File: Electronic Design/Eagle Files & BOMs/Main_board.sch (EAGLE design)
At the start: 36 parts, among them IC1 ACS712ELC-5A, IC2 ATMEGA328-PU, Q1 IRF9540, Q2 IRF9540, X1 16MHz

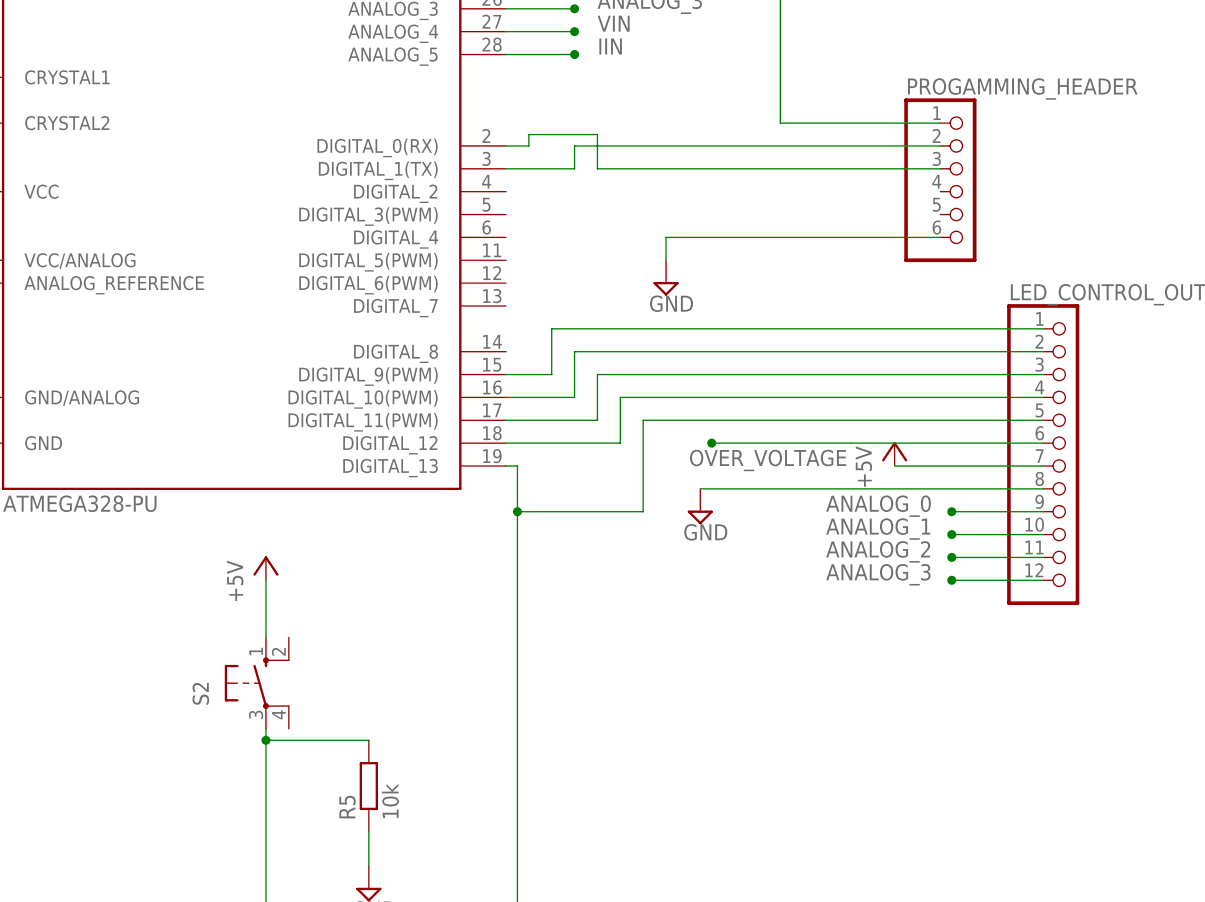
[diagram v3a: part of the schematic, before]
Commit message: adding header for additional DIO pins
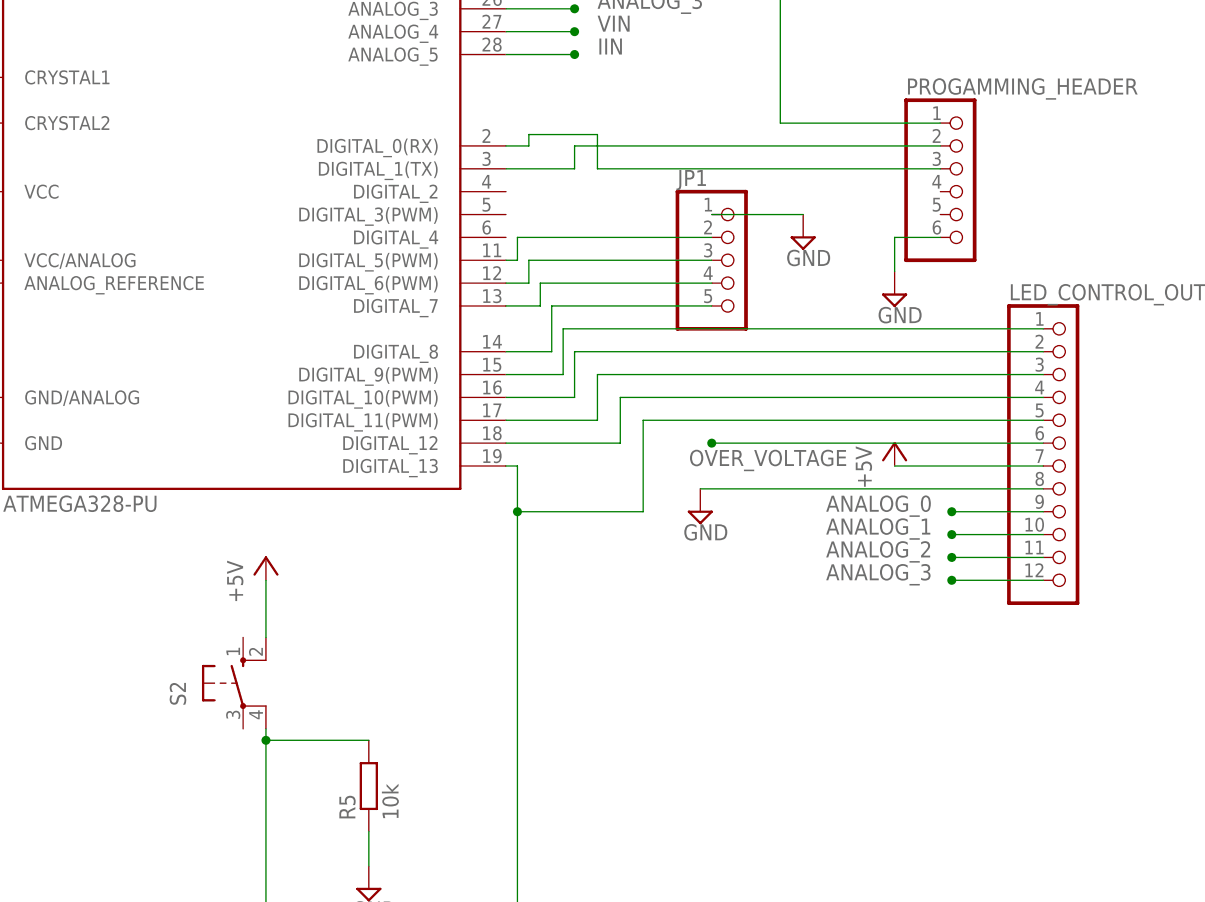
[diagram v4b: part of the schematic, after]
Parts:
- added JP1: (no value), pinhead:PINHD-1X5
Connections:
- new net N$20: IC2.DIGITAL_8, JP1.5
- new net N$21: IC2.DIGITAL_7, JP1.4
- new net N$22: IC2.DIGITAL_6(PWM), JP1.3
- new net N$25: IC2.DIGITAL_5(PWM), JP1.2
- net +5V: now also S2.S1; no longer S2.S
- net GND: now also JP1.1
- net N$8: now also S2.P1; no longer S2.P
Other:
- moved on the sheet: S2
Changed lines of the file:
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@@
 <part name="SUPPLY4" library="supply2" deviceset="GND" device=""/>
 <part name="R6" library="varistor" deviceset="S14K17" device="" value="S14K75"/>
+<part name="JP1" library="pinhead" deviceset="PINHD-1X5" device=""/>
+<part name="SUPPLY5" library="supply2" deviceset="GND" device=""/>
 </parts>
 <sheets>
@@
 <instance part="+3V3" gate="1" x="31.75" y="113.03"/>
 <instance part="PROGAMMING_HEADER" gate="A" x="38.1" y="22.86"/>
-<instance part="SUPPLY6" gate="GND" x="5.08" y="12.7"/>
+<instance part="SUPPLY6" gate="GND" x="30.48" y="11.43"/>
 <instance part="C6" gate="G$1" x="74.93" y="50.8"/>
 <instance part="VIN_BUCK/BOOST" gate="A" x="115.57" y="93.98"/>
@@
 <instance part="R3" gate="G$1" x="77.47" y="99.06"/>
 <instance part="USB_OUT" gate="A" x="93.98" y="87.63"/>
-<instance part="S2" gate="1" x="-39.37" y="-31.75"/>
+<instance part="S2" gate="1" x="-41.91" y="-31.75"/>
 <instance part="+5V2" gate="1" x="-39.37" y="-17.78"/>
 <instance part="R5" gate="G$1" x="-27.94" y="-43.18" rot="R90"/>
@@
 <instance part="SUPPLY4" gate="GND" x="104.14" y="69.85"/>
 <instance part="R6" gate="G$1" x="-97.79" y="88.9" rot="R270"/>
+<instance part="JP1" gate="A" x="12.7" y="15.24"/>
+<instance part="SUPPLY5" gate="GND" x="20.32" y="17.78"/>
 </instances>
 <busses>
@@
 <segment>
 <pinref part="PROGAMMING_HEADER" gate="A" pin="6"/>
-<wire x1="35.56" y1="17.78" x2="5.08" y2="17.78" width="0.1524" layer="91"/>
-<wire x1="5.08" y1="17.78" x2="5.08" y2="15.24" width="0.1524" layer="91"/>
+<wire x1="35.56" y1="17.78" x2="30.48" y2="17.78" width="0.1524" layer="91"/>
+<wire x1="30.48" y1="17.78" x2="30.48" y2="13.97" width="0.1524" layer="91"/>
 <pinref part="SUPPLY6" gate="GND" pin="GND"/>
 </segment>
@@
 <pinref part="VIN_BUCK/BOOST" gate="A" pin="3"/>
 <wire x1="113.03" y1="91.44" x2="104.14" y2="91.44" width="0.1524" layer="91"/>
+</segment>
+<segment>
+<pinref part="JP1" gate="A" pin="1"/>
+<pinref part="SUPPLY5" gate="GND" pin="GND"/>
+<wire x1="10.16" y1="20.32" x2="20.32" y2="20.32" width="0.1524" layer="91"/>
 </segment>
 </net>
@@
 </segment>
 <segment>
-<pinref part="S2" gate="1" pin="S"/>
-<pinref part="+5V2" gate="1" pin="+5V"/>
-<wire x1="-39.37" y1="-26.67" x2="-39.37" y2="-20.32" width="0.1524" layer="91"/>
-</segment>
-<segment>
 <pinref part="+5V3" gate="1" pin="+5V"/>
 <pinref part="LED_CONTROL_OUT" gate="G$1" pin="7"/>
@@
 <wire x1="13.97" y1="105.41" x2="31.75" y2="105.41" width="0.1524" layer="91"/>
 <pinref part="+3V3" gate="1" pin="+5V"/>
+</segment>
+<segment>
+<pinref part="+5V2" gate="1" pin="+5V"/>
+<pinref part="S2" gate="1" pin="S1"/>
+<wire x1="-39.37" y1="-20.32" x2="-39.37" y2="-26.67" width="0.1524" layer="91"/>
 </segment>
 </net>
@@
 <wire x1="-12.7" y1="-7.62" x2="-11.43" y2="-7.62" width="0.1524" layer="91"/>
 <wire x1="-11.43" y1="-7.62" x2="-11.43" y2="-12.7" width="0.1524" layer="91"/>
-<pinref part="S2" gate="1" pin="P"/>
 <wire x1="-11.43" y1="-12.7" x2="-11.43" y2="-68.58" width="0.1524" layer="91"/>
 <wire x1="-11.43" y1="-68.58" x2="-39.37" y2="-68.58" width="0.1524" layer="91"/>
 <wire x1="-39.37" y1="-68.58" x2="-39.37" y2="-38.1" width="0.1524" layer="91"/>
 <pinref part="R5" gate="G$1" pin="2"/>
-<wire x1="-39.37" y1="-38.1" x2="-39.37" y2="-36.83" width="0.1524" layer="91"/>
 <wire x1="-27.94" y1="-38.1" x2="-39.37" y2="-38.1" width="0.1524" layer="91"/>
-<junction x="-39.37" y="-38.1"/>
 <wire x1="2.54" y1="-2.54" x2="2.54" y2="-12.7" width="0.1524" layer="91"/>
 <wire x1="2.54" y1="-12.7" x2="-11.43" y2="-12.7" width="0.1524" layer="91"/>
@@
 <pinref part="LED_CONTROL_OUT" gate="G$1" pin="5"/>
 <wire x1="46.99" y1="-2.54" x2="2.54" y2="-2.54" width="0.1524" layer="91"/>
+<pinref part="S2" gate="1" pin="P1"/>
+<wire x1="-39.37" y1="-36.83" x2="-39.37" y2="-38.1" width="0.1524" layer="91"/>
+<junction x="-39.37" y="-38.1"/>
 </segment>
 </net>
@@
 <segment>
 <pinref part="IC2" gate="1" pin="DIGITAL_9(PWM)"/>
-<wire x1="-12.7" y1="2.54" x2="-7.62" y2="2.54" width="0.1524" layer="91"/>
-<wire x1="-7.62" y1="2.54" x2="-7.62" y2="7.62" width="0.1524" layer="91"/>
+<wire x1="-12.7" y1="2.54" x2="-6.35" y2="2.54" width="0.1524" layer="91"/>
+<wire x1="-6.35" y1="2.54" x2="-6.35" y2="7.62" width="0.1524" layer="91"/>
 <pinref part="LED_CONTROL_OUT" gate="G$1" pin="1"/>
-<wire x1="-7.62" y1="7.62" x2="46.99" y2="7.62" width="0.1524" layer="91"/>
+<wire x1="-6.35" y1="7.62" x2="46.99" y2="7.62" width="0.1524" layer="91"/>
 </segment>
 </net>
@@
 </segment>
 </net>
+<net name="N$20" class="0">
+<segment>
+<pinref part="IC2" gate="1" pin="DIGITAL_8"/>
+<wire x1="-7.62" y1="5.08" x2="-12.7" y2="5.08" width="0.1524" layer="91"/>
+<pinref part="JP1" gate="A" pin="5"/>
+<wire x1="10.16" y1="10.16" x2="-7.62" y2="10.16" width="0.1524" layer="91"/>
+<wire x1="-7.62" y1="10.16" x2="-7.62" y2="5.08" width="0.1524" layer="91"/>
+</segment>
+</net>
+<net name="N$21" class="0">
+<segment>
+<pinref part="IC2" gate="1" pin="DIGITAL_7"/>
+<wire x1="-8.89" y1="10.16" x2="-12.7" y2="10.16" width="0.1524" layer="91"/>
+<wire x1="-8.89" y1="10.16" x2="-8.89" y2="12.7" width="0.1524" layer="91"/>
+<pinref part="JP1" gate="A" pin="4"/>
+<wire x1="-8.89" y1="12.7" x2="10.16" y2="12.7" width="0.1524" layer="91"/>
+</segment>
+</net>
+<net name="N$22" class="0">
+<segment>
+<pinref part="IC2" gate="1" pin="DIGITAL_6(PWM)"/>
+<wire x1="-12.7" y1="12.7" x2="-10.16" y2="12.7" width="0.1524" layer="91"/>
+<wire x1="-10.16" y1="12.7" x2="-10.16" y2="15.24" width="0.1524" layer="91"/>
+<pinref part="JP1" gate="A" pin="3"/>
+<wire x1="-10.16" y1="15.24" x2="10.16" y2="15.24" width="0.1524" layer="91"/>
+</segment>
+</net>
+<net name="N$25" class="0">
+<segment>
+<pinref part="IC2" gate="1" pin="DIGITAL_5(PWM)"/>
+<wire x1="-12.7" y1="15.24" x2="-11.43" y2="15.24" width="0.1524" layer="91"/>
+<wire x1="-11.43" y1="15.24" x2="-11.43" y2="17.78" width="0.1524" layer="91"/>
+<pinref part="JP1" gate="A" pin="2"/>
+<wire x1="-11.43" y1="17.78" x2="10.16" y2="17.78" width="0.1524" layer="91"/>
+</segment>
+</net>

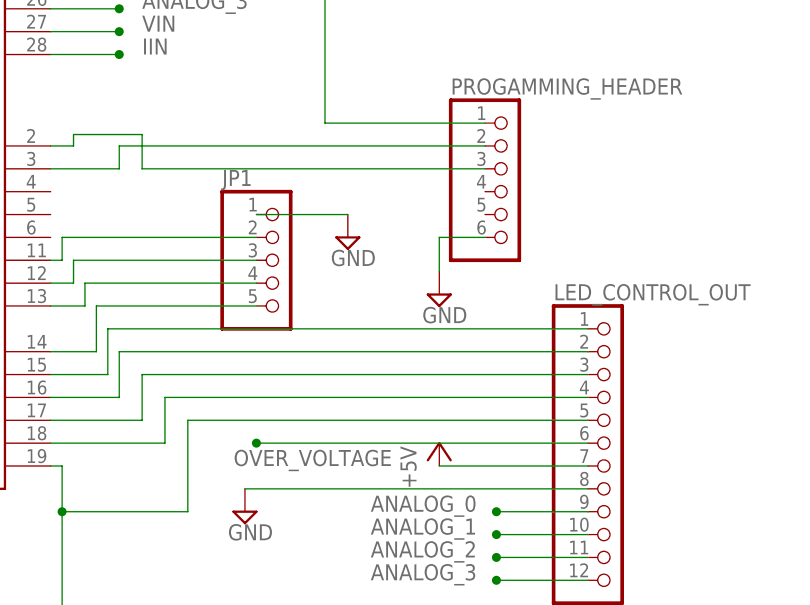
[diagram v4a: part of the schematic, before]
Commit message: fixing minor drc errors and repostionings monting holes
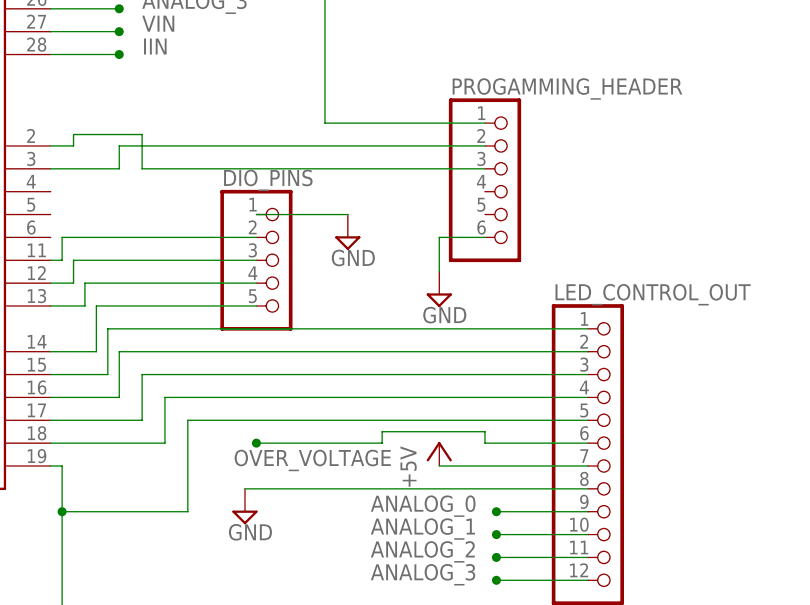
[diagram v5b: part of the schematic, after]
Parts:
- renumbered JP1 to DIO_PINS
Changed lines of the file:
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@@
 <part name="SUPPLY4" library="supply2" deviceset="GND" device=""/>
 <part name="R6" library="varistor" deviceset="S14K17" device="" value="S14K75"/>
-<part name="JP1" library="pinhead" deviceset="PINHD-1X5" device=""/>
+<part name="DIO_PINS" library="pinhead" deviceset="PINHD-1X5" device=""/>
 <part name="SUPPLY5" library="supply2" deviceset="GND" device=""/>
 </parts>
@@
 <instance part="SUPPLY4" gate="GND" x="104.14" y="69.85"/>
 <instance part="R6" gate="G$1" x="-97.79" y="88.9" rot="R270"/>
-<instance part="JP1" gate="A" x="12.7" y="15.24"/>
+<instance part="DIO_PINS" gate="A" x="12.7" y="15.24"/>
 <instance part="SUPPLY5" gate="GND" x="20.32" y="17.78"/>
 </instances>
@@
 </segment>
 <segment>
-<pinref part="JP1" gate="A" pin="1"/>
+<pinref part="DIO_PINS" gate="A" pin="1"/>
 <pinref part="SUPPLY5" gate="GND" pin="GND"/>
 <wire x1="10.16" y1="20.32" x2="20.32" y2="20.32" width="0.1524" layer="91"/>
@@
 <segment>
 <pinref part="LED_CONTROL_OUT" gate="G$1" pin="6"/>
-<wire x1="46.99" y1="-5.08" x2="10.16" y2="-5.08" width="0.1524" layer="91"/>
+<wire x1="46.99" y1="-5.08" x2="35.56" y2="-5.08" width="0.1524" layer="91"/>
 <junction x="10.16" y="-5.08"/>
 <label x="7.62" y="-7.62" size="1.778" layer="95"/>
+<wire x1="24.13" y1="-5.08" x2="10.16" y2="-5.08" width="0.1524" layer="91"/>
+<wire x1="35.56" y1="-5.08" x2="35.56" y2="-3.81" width="0.1524" layer="91"/>
+<wire x1="35.56" y1="-3.81" x2="24.13" y2="-3.81" width="0.1524" layer="91"/>
+<wire x1="24.13" y1="-3.81" x2="24.13" y2="-5.08" width="0.1524" layer="91"/>
 </segment>
 <segment>
@@
 <pinref part="IC2" gate="1" pin="DIGITAL_8"/>
 <wire x1="-7.62" y1="5.08" x2="-12.7" y2="5.08" width="0.1524" layer="91"/>
-<pinref part="JP1" gate="A" pin="5"/>
+<pinref part="DIO_PINS" gate="A" pin="5"/>
 <wire x1="10.16" y1="10.16" x2="-7.62" y2="10.16" width="0.1524" layer="91"/>
 <wire x1="-7.62" y1="10.16" x2="-7.62" y2="5.08" width="0.1524" layer="91"/>
@@
 <wire x1="-8.89" y1="10.16" x2="-12.7" y2="10.16" width="0.1524" layer="91"/>
 <wire x1="-8.89" y1="10.16" x2="-8.89" y2="12.7" width="0.1524" layer="91"/>
-<pinref part="JP1" gate="A" pin="4"/>
+<pinref part="DIO_PINS" gate="A" pin="4"/>
 <wire x1="-8.89" y1="12.7" x2="10.16" y2="12.7" width="0.1524" layer="91"/>
 </segment>
@@
 <wire x1="-12.7" y1="12.7" x2="-10.16" y2="12.7" width="0.1524" layer="91"/>
 <wire x1="-10.16" y1="12.7" x2="-10.16" y2="15.24" width="0.1524" layer="91"/>
-<pinref part="JP1" gate="A" pin="3"/>
+<pinref part="DIO_PINS" gate="A" pin="3"/>
 <wire x1="-10.16" y1="15.24" x2="10.16" y2="15.24" width="0.1524" layer="91"/>
 </segment>
@@
 <wire x1="-12.7" y1="15.24" x2="-11.43" y2="15.24" width="0.1524" layer="91"/>
 <wire x1="-11.43" y1="15.24" x2="-11.43" y2="17.78" width="0.1524" layer="91"/>
-<pinref part="JP1" gate="A" pin="2"/>
+<pinref part="DIO_PINS" gate="A" pin="2"/>
 <wire x1="-11.43" y1="17.78" x2="10.16" y2="17.78" width="0.1524" layer="91"/>
 </segment>

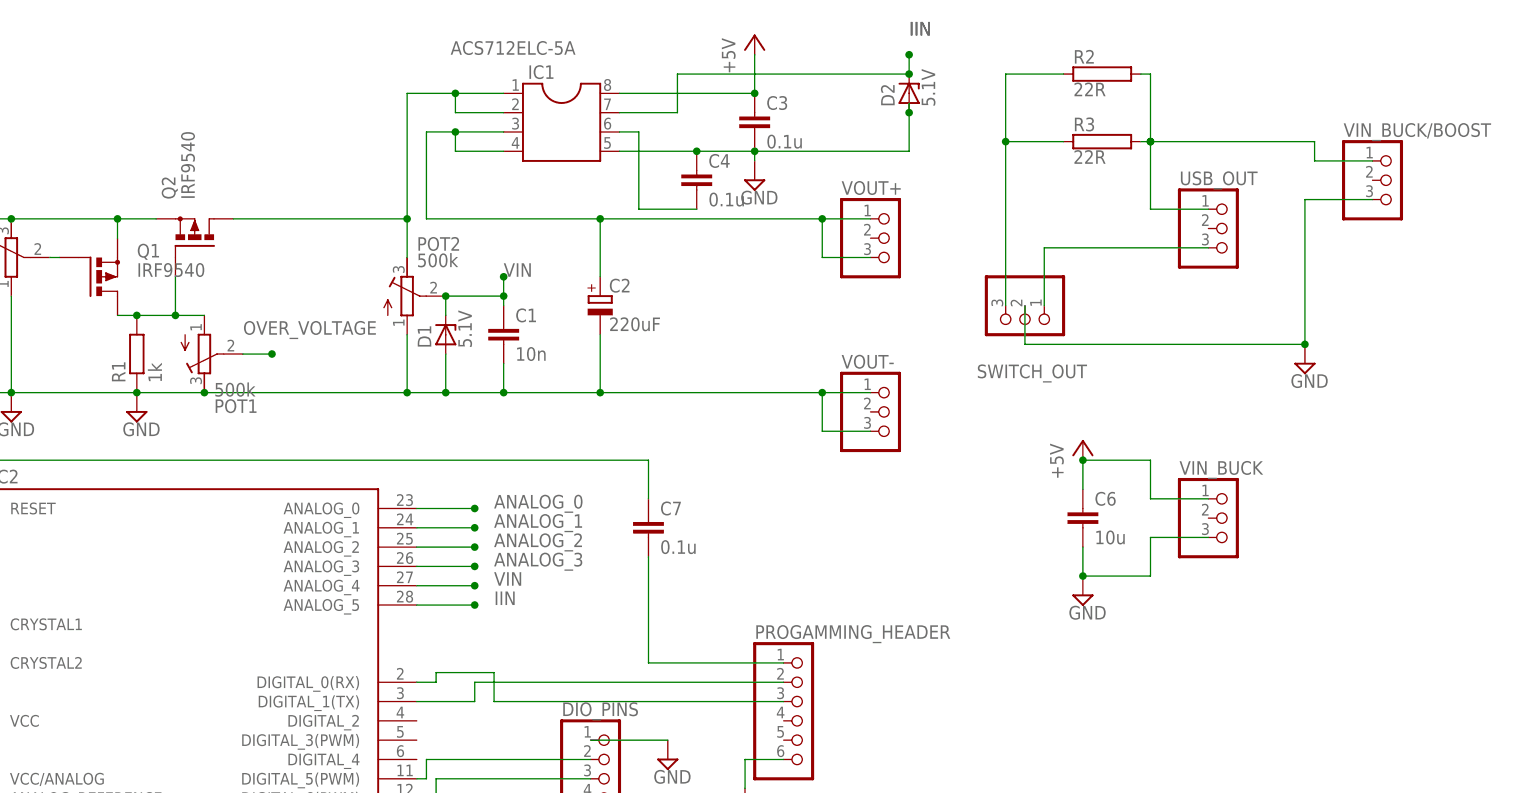
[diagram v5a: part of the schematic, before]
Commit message: removing dummy load and adding in lm2596 boards to PCB
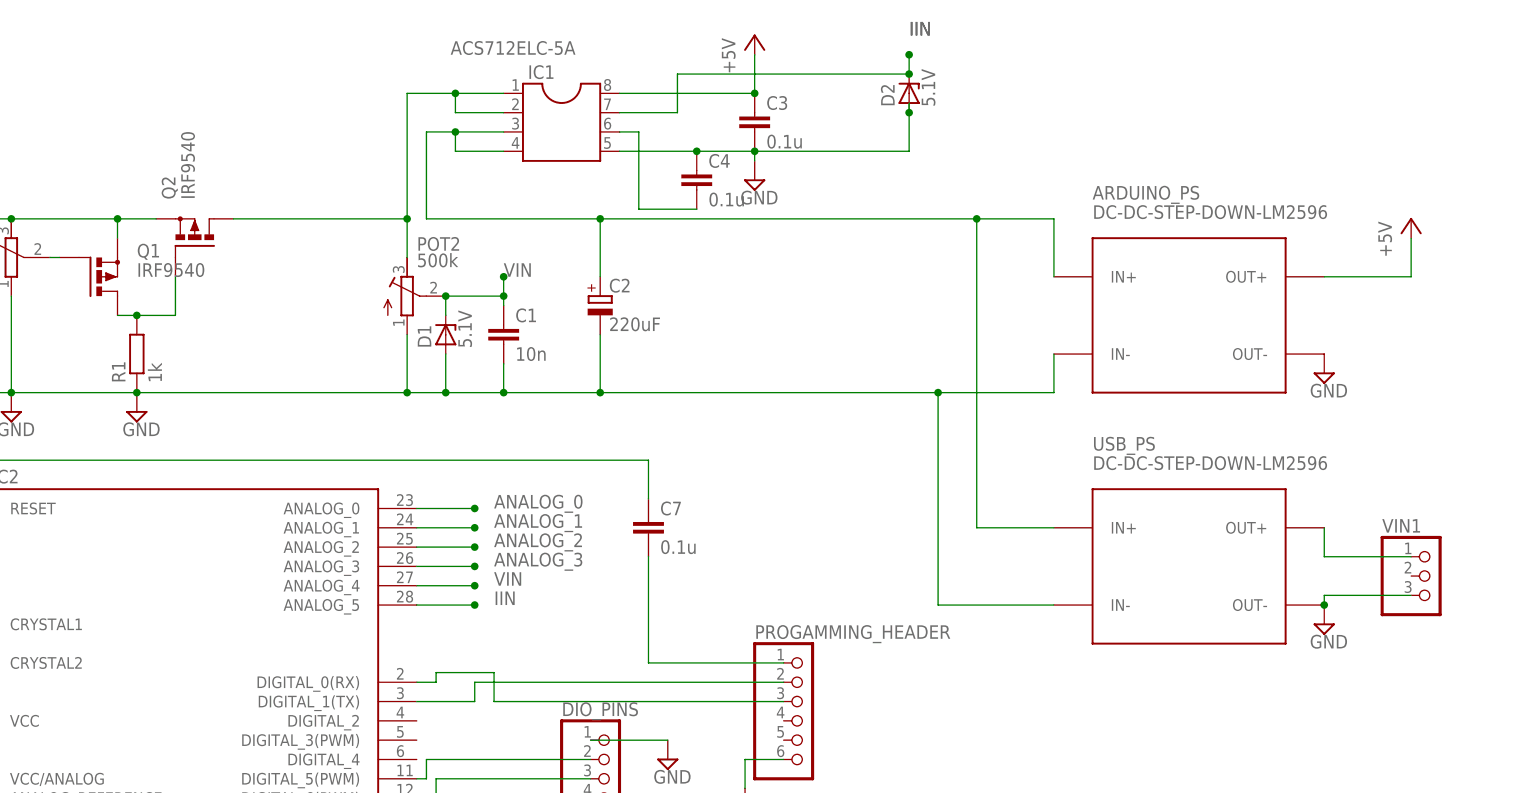
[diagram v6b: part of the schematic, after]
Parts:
- removed C6: 10u, resistor:C-EUC1206K
- removed POT1: 500k, resistor:R-TRIMM3296W
- removed R2, R3: 22R, resistor-power:RRWM8X45
- removed SWITCH_OUT, USB_OUT, VIN_BUCK, VIN_BUCK/BOOST, VOUT+, VOUT-: (no value), pinhead:PINHD-1X3
- added ARDUINO_PS, USB_PS: DC-DC-STEP-DOWN-LM2596, diy-modules:DC-DC-STEP-DOWN-LM2596
- added VIN1: (no value), pinhead:PINHD-1X3
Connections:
- removed net N$23: R2.2, R3.2, USB_OUT.1, VIN_BUCK/BOOST.1
- removed net N$24: R2.1, R3.1, SWITCH_OUT.3
- net +5V: now also ARDUINO_PS.OUT+; no longer C6.1, VIN_BUCK.1
- net GND: now also ARDUINO_PS.IN-, ARDUINO_PS.OUT-, USB_PS.IN-, USB_PS.OUT-, VIN1.3; no longer C6.2, POT1.E, SWITCH_OUT.2, VIN_BUCK.3, VIN_BUCK/BOOST.3, VOUT-.1, VOUT-.3
- net M1S: now also ARDUINO_PS.IN+, USB_PS.IN+; no longer VOUT+.1, VOUT+.3
- net N$13: now also USB_PS.OUT+, VIN1.1; no longer SWITCH_OUT.1, USB_OUT.3
- net N$35: no longer POT1.A
- net OVER_VOLTAGE: no longer POT1.S

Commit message: Tidying up names
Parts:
- removed ARDUINO_PS: DC-DC-STEP-DOWN-LM2596, diy-modules:DC-DC-STEP-DOWN-LM2596
- removed VIN1: (no value), pinhead:PINHD-1X3
- added ATMEGA_PS: DC-DC-STEP-DOWN-LM2596, diy-modules:DC-DC-STEP-DOWN-LM2596
- added VOUT: (no value), pinhead:PINHD-1X3
- renumbered LED_CONTROL_OUT to ATMEGA_AIO_DIO
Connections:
- net +5V: now also ATMEGA_PS.OUT+; no longer ARDUINO_PS.OUT+
- net GND: now also ATMEGA_PS.IN-, ATMEGA_PS.OUT-, VOUT.3; no longer ARDUINO_PS.IN-, ARDUINO_PS.OUT-, VIN1.3
- net M1S: now also ATMEGA_PS.IN+; no longer ARDUINO_PS.IN+
- net N$13: now also VOUT.1; no longer VIN1.1
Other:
- moved on the sheet: USB_PS
